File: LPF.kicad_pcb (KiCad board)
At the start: 4 copper layers, 100 x 100 mm, 601 parts, among them J1 Conn_02x05_Counter_Clockwise, P1 SMA, P2 SMA, P3 SMA, P4 SMA, P5 SMA, P6 SMA

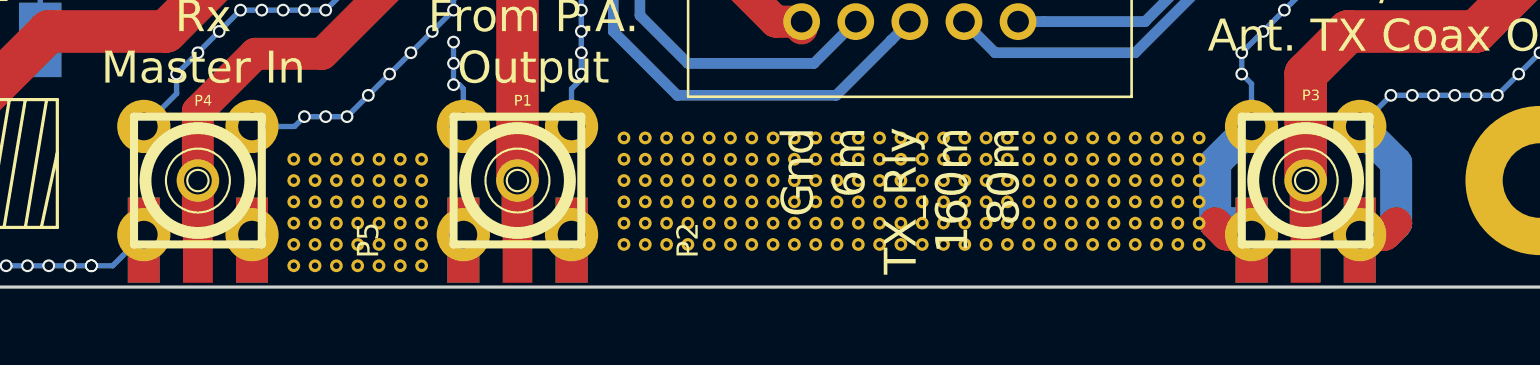
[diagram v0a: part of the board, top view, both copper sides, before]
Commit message: upgrate to Kicad 5.0n, new up to date Gerber
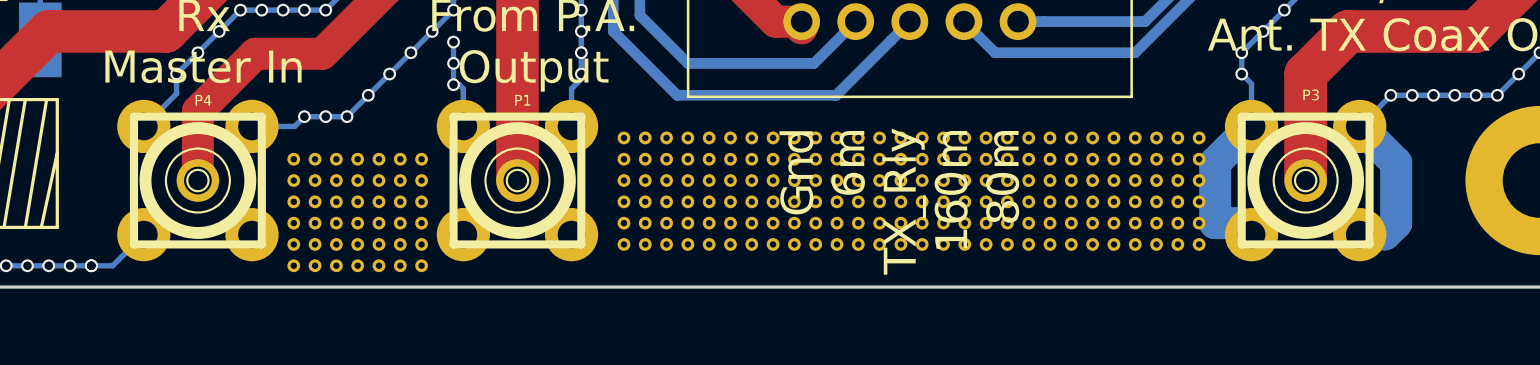
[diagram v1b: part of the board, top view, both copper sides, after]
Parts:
- removed P2, P5, P6: SMA, SMA_PINS:SMA_EDGE_NRW
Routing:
- net GND: track 1547.3 -> 1543.4 mm
- net Net-(P4-Pad1): track 25.8 -> 23.8 mm
- net Net-(P3-Pad1): track 106.4 -> 104.4 mm
- net Net-(P1-Pad1): track 19.9 -> 17.9 mm

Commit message: V 3.0, 54 MHz lpf now online
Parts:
- removed C69: 18p, ATC_B:ATC_500_HandSoldering
- removed REF** (x459): via, via:via
- C11, C27: value C -> 120p
- C16, C18, C29, C41: value C -> 39p
- C17: value 24p -> 4.7p
- C19: value C -> 1000p
- C20, C25: value C -> 470p
- C21: value C -> 330p
- C22, C50, C55: value C -> 82p
- C23, C40: value C -> 68p
- C24: value 31p -> 56p
- C26: value C -> 240p
- C28: value C -> 56p
- C30: value 15p -> 12p
- C31, C35, C36: value C -> 220p
- C32: value C -> 2200p
- C33, C46: value C -> 1100p
- C34: value C -> 680p
- C37, C42: value C -> 180p
- C38: value 68p -> 56p
- C39, C51: value C -> 150p
- C43: value C -> 22p
- C44: value C -> 6.8p
- C45: value 4.7 -> 4.7p
- C47: value C -> 560p
- C48: value C -> 390p
- C49: value C -> 100p
- C59: value 24p -> C (nc)
- L1: value L -> 562nH
- L10: value L -> 4.4uH
- L11: value L -> 2.02uH
- L12: value L -> 1.36uH
- L13: value L -> 351nH
- L14, L16, L6, L9: value L -> 311nH
- L15, L2: value L -> 169nH
- L3: value L -> 3.5uH
- L4: value L -> 1,66uH
- L5: value L -> 1.18uH
- L7: value L -> 235nH
- L8: value L -> 196nH
- moved C59 57.6 mm to (126.5, 117.0), turned to 90 degrees
- moved L15 57.0 mm to (123.0, 119.0), turned to 0 degrees
- moved C45 53.8 mm to (117.5, 120.5), turned to 270 degrees
- moved C15 50.1 mm to (75.0, 116.5), turned to 270 degrees
- moved RL8 50.0 mm to (70.0, 119.0)
- moved D9 49.5 mm to (78.0, 119.0)
- moved L30 43.2 mm to (81.0, 120.0)
- moved C38 40.5 mm to (113.0, 116.5), turned to 270 degrees
- moved L8 34.6 mm to (104.5, 120.0), turned to 45 degrees
- moved C30 27.9 mm to (93.0, 116.5), turned to 0 degrees
- moved RL1 25.9 mm to (66.5, 130.5)
- moved L2 25.2 mm to (87.0, 118.0), turned to 0 degrees
- moved D1 24.3 mm to (60.5, 130.0)
- moved C7 23.7 mm to (63.5, 126.5), turned to 90 degrees
- moved L17 23.0 mm to (68.0, 130.0)
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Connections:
- RL1 pad 13: Net-(C17-Pad1) -> Net-(RL1-Pad13)
- RL1 pad 4: Net-(C17-Pad1) -> Net-(RL1-Pad13)
- RL15 pad 13: Net-(C69-Pad1) -> Net-(C45-Pad2)
- RL15 pad 4: Net-(C69-Pad1) -> Net-(C45-Pad2)
- RL2 pad 8: Net-(C45-Pad2) -> Net-(RL1-Pad13)
- RL2 pad 9: Net-(C45-Pad2) -> Net-(RL1-Pad13)
- RL3 pad 8: Net-(C45-Pad2) -> Net-(RL1-Pad13)
- RL3 pad 9: Net-(C45-Pad2) -> Net-(RL1-Pad13)
- RL4 pad 8: Net-(C45-Pad2) -> Net-(RL1-Pad13)
- RL4 pad 9: Net-(C45-Pad2) -> Net-(RL1-Pad13)
- RL5 pad 8: Net-(C45-Pad2) -> Net-(RL1-Pad13)
- RL5 pad 9: Net-(C45-Pad2) -> Net-(RL1-Pad13)
- RL6 pad 8: Net-(C45-Pad2) -> Net-(RL1-Pad13)
- RL6 pad 9: Net-(C45-Pad2) -> Net-(RL1-Pad13)
- RL7 pad 8: Net-(C45-Pad2) -> Net-(RL1-Pad13)
- RL7 pad 9: Net-(C45-Pad2) -> Net-(RL1-Pad13)
- RL8 pad 13: Net-(C69-Pad1) -> Net-(C17-Pad1)
- RL8 pad 4: Net-(C69-Pad1) -> Net-(C17-Pad1)
- RL8 pad 8: Net-(C45-Pad2) -> Net-(RL1-Pad13)
- RL8 pad 9: Net-(C45-Pad2) -> Net-(RL1-Pad13)
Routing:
- net GND: track 1543.4 -> 568.0 mm, vias 769 -> 1045
- net Net-(C45-Pad2): track 137.5 -> 35.5 mm
- net Net-(RL1-Pad13): track 0.00 -> 94.5 mm
- net Net-(C69-Pad1): track 46.1 -> 0.00 mm
- net 6m_Bypass: track 50.6 -> 81.4 mm
- net +12V: track 93.2 -> 69.0 mm
- net Net-(C30-Pad2): track 17.2 -> 41.2 mm
- net Net-(P1-Pad1): track 17.9 -> 38.5 mm
- net TX_RX_RLY: track 44.8 -> 55.7 mm
- net Net-(C17-Pad2): track 20.7 -> 26.8 mm
- net Net-(P4-Pad1): track 23.8 -> 27.0 mm
- net Net-(C17-Pad1): track 33.6 -> 32.2 mm
- net Net-(C15-Pad1): track 7.26 -> 8.21 mm
- net (no net): vias 0 -> 6
- added copper zone on F.Cu, net GND
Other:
- board text added: "Alexiares LPF V3.0"
- board text removed: "Alexiares LPF V2.0"

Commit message: version 3 provisoire
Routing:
- net GND: vias 1045 -> 1084
- net (no net): vias 6 -> 1
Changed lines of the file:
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@@
-(kicad_pcb (version 20171130) (host pcbnew "(5.0.2)-1")
+(kicad_pcb (version 20171130) (host pcbnew "(5.1.2)-2")
   (general
     (thickness 1.6)
     (drawings 26)
-    (tracks 1917)
+    (tracks 1951)
     (zones 0)
     (modules 138)
@@
   )
   (setup
-    (last_trace_width 3)
+    (last_trace_width 0.25)
     (user_trace_width 0.5)
     (user_trace_width 0.7)
@@
     (zone_45_only no)
     (trace_min 0.2)
-    (segment_width 0.2)
-    (edge_width 0.15)
     (via_size 0.6)
     (via_drill 0.4)
@@
     (uvia_min_size 0.2)
     (uvia_min_drill 0.1)
+    (edge_width 0.15)
+    (segment_width 0.2)
     (pcb_text_width 0.3)
     (pcb_text_size 1.5 1.5)
@@
     (visible_elements 7FFFFE49)
     (pcbplotparams
-      (layerselection 0x010f0_80000007)
+      (layerselection 0x010f0_ffffffff)
       (usegerberextensions true)
       (usegerberattributes false)
       (usegerberadvancedattributes false)
       (creategerberjobfile false)
-      (excludeedgelayer true)
+      (excludeedgelayer false)
       (linewidth 0.100000)
       (plotframeref false)
@@
       (drillshape 0)
       (scaleselection 1)
-      (outputdirectory "Gerber_V2/"))
+      (outputdirectory "Gerber_V3/"))
   )
   (net 0 "")
@@
   (gr_line (start 155 45) (end 55 45) (angle 90) (layer Edge.Cuts) (width 0.15))
   (gr_line (start 155 145) (end 155 45) (angle 90) (layer Edge.Cuts) (width 0.15))
+  (via (at 126 69.5) (size 0.6) (drill 0.4) (layers F.Cu B.Cu) (net 0))
   (via (at 98 113.5) (size 0.6) (drill 0.4) (layers F.Cu B.Cu) (net 1))
   (via (at 99 113.5) (size 0.6) (drill 0.4) (layers F.Cu B.Cu) (net 1))
@@
   (via (at 102 113.5) (size 0.6) (drill 0.4) (layers F.Cu B.Cu) (net 1))
   (via (at 103 113.5) (size 0.6) (drill 0.4) (layers F.Cu B.Cu) (net 1))
-  (via (at 124 125) (size 0.6) (drill 0.4) (layers F.Cu B.Cu) (net 0))
-  (via (at 125 125) (size 0.6) (drill 0.4) (layers F.Cu B.Cu) (net 0))
-  (via (at 126 125) (size 0.6) (drill 0.4) (layers F.Cu B.Cu) (net 0))
-  (via (at 127 125) (size 0.6) (drill 0.4) (layers F.Cu B.Cu) (net 0))
-  (via (at 128 125) (size 0.6) (drill 0.4) (layers F.Cu B.Cu) (net 0))
-  (via (at 126 69.5) (size 0.6) (drill 0.4) (layers F.Cu B.Cu) (net 0))
   (via (at 86 102.25) (size 0.6) (drill 0.4) (layers F.Cu B.Cu) (net 1))
   (via (at 128 92.25) (size 0.6) (drill 0.4) (layers F.Cu B.Cu) (net 1))
@@
   (segment (start 63.5 124.23) (end 64.92 122.81) (width 1) (layer B.Cu) (net 1))
   (segment (start 63.5 125.25) (end 63.5 124.23) (width 1) (layer B.Cu) (net 1))
-  (via (at 129 121) (size 0.6) (drill 0.4) (layers F.Cu B.Cu) (net 1))
   (via (at 129 122) (size 0.6) (drill 0.4) (layers F.Cu B.Cu) (net 1))
   (via (at 129 123) (size 0.6) (drill 0.4) (layers F.Cu B.Cu) (net 1))
   (via (at 129 124) (size 0.6) (drill 0.4) (layers F.Cu B.Cu) (net 1))
-  (via (at 130 125) (size 0.6) (drill 0.4) (layers F.Cu B.Cu) (net 1))
-  (via (at 131 125) (size 0.6) (drill 0.4) (layers F.Cu B.Cu) (net 1))
-  (via (at 132 125) (size 0.6) (drill 0.4) (layers F.Cu B.Cu) (net 1))
-  (via (at 129 125) (size 0.6) (drill 0.4) (layers F.Cu B.Cu) (net 1))
+  (via (at 130 124.75) (size 0.6) (drill 0.4) (layers F.Cu B.Cu) (net 1))
+  (via (at 131 124.75) (size 0.6) (drill 0.4) (layers F.Cu B.Cu) (net 1))
+  (via (at 132 124.75) (size 0.6) (drill 0.4) (layers F.Cu B.Cu) (net 1))
   (via (at 80 125) (size 0.6) (drill 0.4) (layers F.Cu B.Cu) (net 1))
   (via (at 80 126) (size 0.6) (drill 0.4) (layers F.Cu B.Cu) (net 1))
@@
   (via (at 120 126) (size 0.6) (drill 0.4) (layers F.Cu B.Cu) (net 1))
   (via (at 121 126) (size 0.6) (drill 0.4) (layers F.Cu B.Cu) (net 1))
-  (via (at 122 125) (size 0.6) (drill 0.4) (layers F.Cu B.Cu) (net 1))
-  (via (at 123 125) (size 0.6) (drill 0.4) (layers F.Cu B.Cu) (net 1))
+  (via (at 122 125.5) (size 0.6) (drill 0.4) (layers F.Cu B.Cu) (net 1))
+  (via (at 123.25 124.75) (size 0.6) (drill 0.4) (layers F.Cu B.Cu) (net 1))
   (via (at 78.75 124.75) (size 0.6) (drill 0.4) (layers F.Cu B.Cu) (net 1))
   (via (at 77.5 124.75) (size 0.6) (drill 0.4) (layers F.Cu B.Cu) (net 1))
@@
   (via (at 127 112.5) (size 0.6) (drill 0.4) (layers F.Cu B.Cu) (net 1))
   (via (at 129 112) (size 0.6) (drill 0.4) (layers F.Cu B.Cu) (net 1))
+  (via (at 91 104.25) (size 0.6) (drill 0.4) (layers F.Cu B.Cu) (net 1))
+  (via (at 80 104.75) (size 0.6) (drill 0.4) (layers F.Cu B.Cu) (net 1))
+  (via (at 81 104.75) (size 0.6) (drill 0.4) (layers F.Cu B.Cu) (net 1))
+  (via (at 82 104.75) (size 0.6) (drill 0.4) (layers F.Cu B.Cu) (net 1))
+  (via (at 83 104.75) (size 0.6) (drill 0.4) (layers F.Cu B.Cu) (net 1))
+  (via (at 84 104.75) (size 0.6) (drill 0.4) (layers F.Cu B.Cu) (net 1))
+  (via (at 85 104.75) (size 0.6) (drill 0.4) (layers F.Cu B.Cu) (net 1))
+  (via (at 92 104.25) (size 0.6) (drill 0.4) (layers F.Cu B.Cu) (net 1))
+  (via (at 93 104.25) (size 0.6) (drill 0.4) (layers F.Cu B.Cu) (net 1))
+  (via (at 94 104.25) (size 0.6) (drill 0.4) (layers F.Cu B.Cu) (net 1))
+  (via (at 95 104.25) (size 0.6) (drill 0.4) (layers F.Cu B.Cu) (net 1))
+  (via (at 96 104.25) (size 0.6) (drill 0.4) (layers F.Cu B.Cu) (net 1))
+  (via (at 97 104.25) (size 0.6) (drill 0.4) (layers F.Cu B.Cu) (net 1))
+  (via (at 98 104.25) (size 0.6) (drill 0.4) (layers F.Cu B.Cu) (net 1))
+  (via (at 99 104.25) (size 0.6) (drill 0.4) (layers F.Cu B.Cu) (net 1))
+  (via (at 100 104.25) (size 0.6) (drill 0.4) (layers F.Cu B.Cu) (net 1))
+  (via (at 101 104.25) (size 0.6) (drill 0.4) (layers F.Cu B.Cu) (net 1))
+  (via (at 102 104.25) (size 0.6) (drill 0.4) (layers F.Cu B.Cu) (net 1))
+  (via (at 103 104.25) (size 0.6) (drill 0.4) (layers F.Cu B.Cu) (net 1))
+  (via (at 104 104.25) (size 0.6) (drill 0.4) (layers F.Cu B.Cu) (net 1))
+  (via (at 105 104.25) (size 0.6) (drill 0.4) (layers F.Cu B.Cu) (net 1))
+  (via (at 106 104.25) (size 0.6) (drill 0.4) (layers F.Cu B.Cu) (net 1))
+  (via (at 107 104.25) (size 0.6) (drill 0.4) (layers F.Cu B.Cu) (net 1))
+  (via (at 108 104.25) (size 0.6) (drill 0.4) (layers F.Cu B.Cu) (net 1))
+  (via (at 109 104.25) (size 0.6) (drill 0.4) (layers F.Cu B.Cu) (net 1))
+  (via (at 110 104.25) (size 0.6) (drill 0.4) (layers F.Cu B.Cu) (net 1))
+  (via (at 111 104.25) (size 0.6) (drill 0.4) (layers F.Cu B.Cu) (net 1))
+  (via (at 112 104.25) (size 0.6) (drill 0.4) (layers F.Cu B.Cu) (net 1))
+  (via (at 113 104.25) (size 0.6) (drill 0.4) (layers F.Cu B.Cu) (net 1))
+  (via (at 114 104.25) (size 0.6) (drill 0.4) (layers F.Cu B.Cu) (net 1))
+  (via (at 119 104.25) (size 0.6) (drill 0.4) (layers F.Cu B.Cu) (net 1))
+  (via (at 120 104.25) (size 0.6) (drill 0.4) (layers F.Cu B.Cu) (net 1))
+  (via (at 121 104.25) (size 0.6) (drill 0.4) (layers F.Cu B.Cu) (net 1))
+  (via (at 122 104.25) (size 0.6) (drill 0.4) (layers F.Cu B.Cu) (net 1))
+  (via (at 123 104.25) (size 0.6) (drill 0.4) (layers F.Cu B.Cu) (net 1))
+  (via (at 124 104.25) (size 0.6) (drill 0.4) (layers F.Cu B.Cu) (net 1))
+  (via (at 125 104.25) (size 0.6) (drill 0.4) (layers F.Cu B.Cu) (net 1))
+  (via (at 124.5 124.75) (size 0.6) (drill 0.4) (layers F.Cu B.Cu) (net 1))
+  (via (at 125.75 124.75) (size 0.6) (drill 0.4) (layers F.Cu B.Cu) (net 1))
+  (via (at 127 124.75) (size 0.6) (drill 0.4) (layers F.Cu B.Cu) (net 1))
+  (via (at 128 124) (size 0.6) (drill 0.4) (layers F.Cu B.Cu) (net 1))
   (segment (start 85.6 59) (end 125.6 59) (width 0.5) (layer B.Cu) (net 2) (status 10))
   (segment (start 131.95 57.2) (end 136.75 62) (width 0.5) (layer B.Cu) (net 2) (status 20))

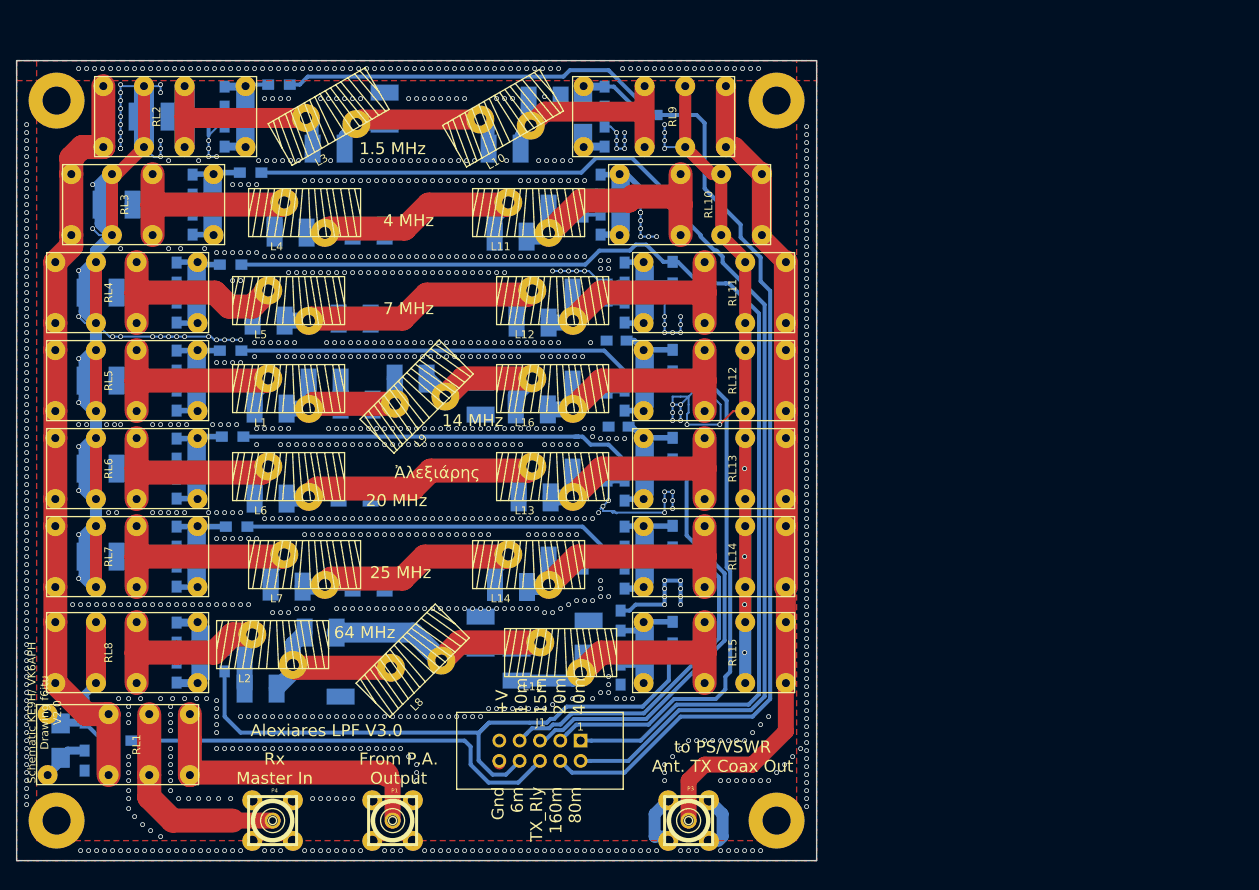
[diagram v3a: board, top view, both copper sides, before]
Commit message: version 4 en dimension 10x15
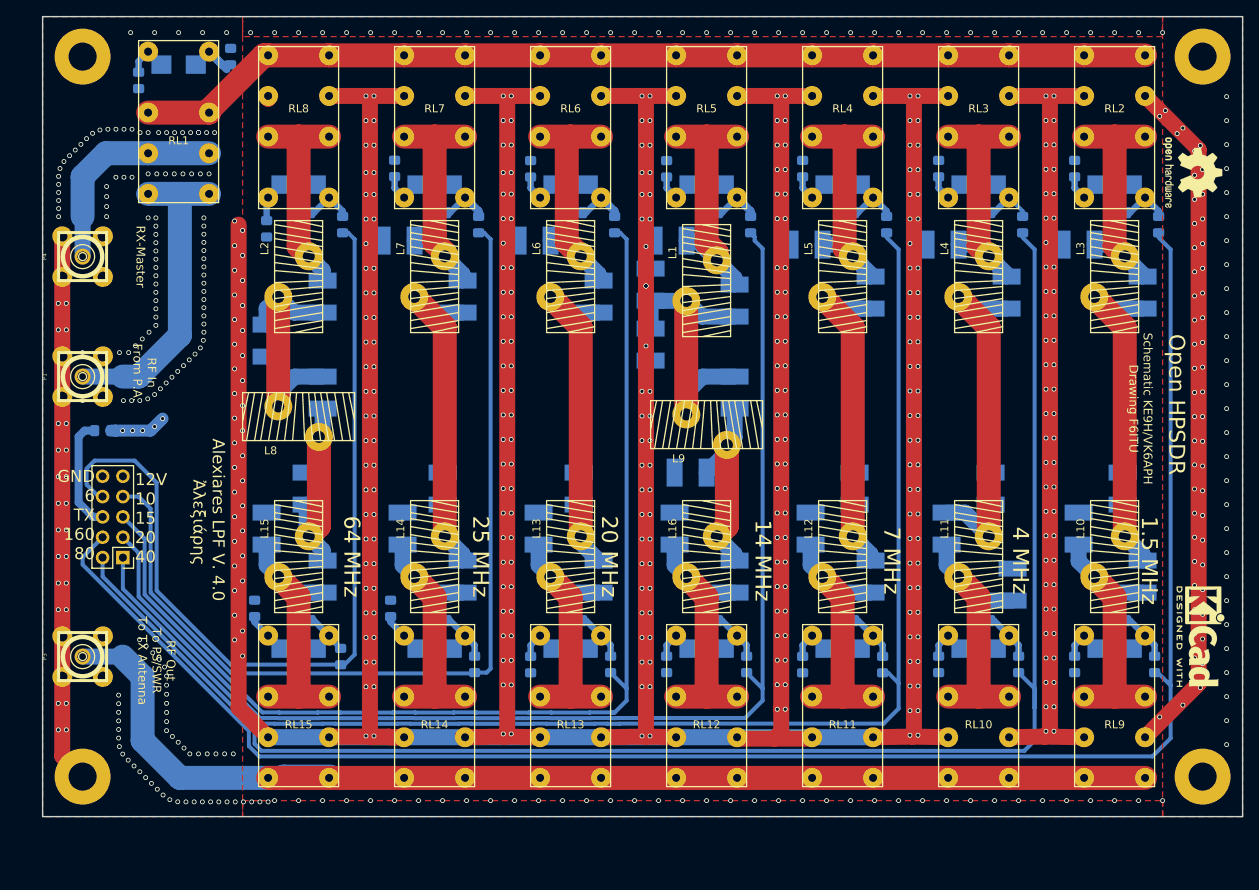
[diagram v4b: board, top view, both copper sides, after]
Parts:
- added REF**: KiCad-Logo2_5mm_SilkScreen, Symbol:KiCad-Logo2_5mm_SilkScreen, F.Cu at (203.0, 117.0)
- added REF**: OSHW-Logo2_9.8x8mm_SilkScreen, Symbol:OSHW-Logo2_9.8x8mm_SilkScreen, F.Cu at (202.0, 59.0)
- C1, C10, C12, C13, C14, C15, C2, C3, C4, C5, C52, C53, C54, C56, C57, C58, C6, C60, C61, C62, C63, C64, C65, C66, C67, C68, C7, C70, C8, C9: footprint Capacitors_SMD:C_0805_HandSoldering -> Capacitor_SMD:C_0805_2012Metric_Pad1.15x1.40mm_HandSolder
- D1, D10, D11, D12, D13, D14, D15, D2, D3, D4, D5, D6, D7, D8, D9: footprint Diodes_SMD:D_SMB -> Diode_SMD:D_SMB
- J1: value Conn_02x05_Counter_Clockwise -> (none); footprint Connectors:IDC_Header_Straight_10pins -> Connector_PinHeader_2.54mm:PinHeader_2x05_P2.54mm_Vertical
- L17, L24, L25, L26, L27, L28, L29, L30, L31, L32, L33, L34, L35, L36, L37: footprint Inductors_SMD:L_0805_HandSoldering -> Inductor_SMD:L_0805_2012Metric_Pad1.15x1.40mm_HandSolder
- TP1, TP2, TP3, TP4: footprint Mounting_Holes:MountingHole_3.5mm_Pad -> MountingHole:MountingHole_3.5mm_Pad
- moved TP3 143.4 mm to (203.2, 134.5), turned to 270 degrees
- moved C61 123.2 mm to (187.2, 120.5), turned to 270 degrees
- moved TP4 121.1 mm to (63.2, 134.5), turned to 270 degrees
- moved C19 116.9 mm to (187.8, 68.0)
- moved RL2 116.3 mm to (192.2, 54.5), turned to 180 degrees
- moved C1 112.7 mm to (192.7, 64.0), turned to 180 degrees
- moved L24 111.3 mm to (197.8, 65.5), turned to 270 degrees
- moved TP2 109.3 mm to (203.2, 44.5), turned to 270 degrees
- moved D3 109.0 mm to (192.2, 60.5), turned to 0 degrees
- moved C8 106.3 mm to (187.2, 58.5)
- moved C32 103.8 mm to (193.2, 98.5)
- moved RL3 103.6 mm to (175.2, 54.5), turned to 180 degrees
- moved C20 103.4 mm to (170.8, 68.0)
- moved C25 103.3 mm to (195.8, 74.0), turned to 270 degrees
- moved L3 100.3 mm to (192.2, 72.0), turned to 270 degrees
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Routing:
- net +12V: track 69.0 -> 475.6 mm
- net GND: track 568.0 -> 894.9 mm, vias 1084 -> 667
- net Net-(C7-Pad1): track 9.22 -> 72.4 mm, vias 0 -> 5
- net 160m: track 161.4 -> 218.9 mm
- net 80m: track 147.8 -> 198.9 mm
- net Net-(P3-Pad1): track 104.4 -> 151.7 mm
- net TX_RX_RLY: track 55.7 -> 14.3 mm
- net Net-(RL1-Pad13): track 94.5 -> 127.8 mm
- net 30/20m: track 124.2 -> 155.4 mm
- net 17/15m: track 110.1 -> 140.2 mm
- net 6m_Bypass: track 81.4 -> 111.3 mm
- net 40m: track 141.6 -> 171.4 mm
- net Net-(C25-Pad2): track 27.0 -> 46.2 mm
- net Net-(C30-Pad2): track 41.2 -> 24.5 mm
- net 12/10m: track 100.5 -> 117.0 mm
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- removed copper zone on In2.Cu, net +12V
- removed copper zone on In1.Cu, net GND
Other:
- board size 100 x 100 mm -> 150 x 100 mm
- board text added: "1.5 MHz 4 MHz 7 MHz 14 MHz"
- board text added: "12V 10 15 20 40"
- board text added: "20 MHz 25 MHz 64 MHz"
- board text added: "Alexiares LPF V. 4.0 Ἀλεξιάρης"
- board text added: "GND 6 TX 160 80"
- board text added: "Open HPSDR"
- board text added: "RF In From P.A."
- board text added: "RF Out To PS/SWR To TX Antenna"
- board text added: "RX-Master"
- board text added: "Schematic KE9H/VK6APH Drawing F6ITU"
- board text removed: "+V 10m 15m 20m 40m"
- board text removed: "1.5 MHz"
- board text removed: "12 Vcc 10m 15m 20m 40m"
- board text removed: "14 MHz"
- board text removed: "20 MHz"
- board text removed: "25 MHz"
- board text removed: "4 MHz"
- board text removed: "64 MHz"
- board text removed: "7 MHz"
- board text removed: "Alexiares LPF"
- board text removed: "Alexiares LPF V3.0"
- board text removed: "From P.A. Output"
- board text removed: "Gnd 6m TX_Rly 160m 80m"
- board text removed: "Gnd 6m-BP TX_Rly 160m 80m"
- board text removed: "RX MASTER_IN"
- board text removed: "Rx Master In"
- board text removed: "Schematic KE9H/ VK6APH Drawing f6itu V2.0"
- board text removed: "to PS/VSWR Ant. TX Coax Out"
- board text removed: "Ἀλεξιάρης"

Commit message: new routing enhancing eddy currents
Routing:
- net GND: track 894.9 -> 885.4 mm, vias 667 -> 665
- net 12/10m: track 117.0 -> 120.4 mm, vias 0 -> 2
- net 160m: track 218.9 -> 221.6 mm, vias 0 -> 3
- net 80m: track 198.9 -> 196.3 mm, vias 0 -> 2
- net 17/15m: track 140.2 -> 140.6 mm, vias 0 -> 2
- net 6m_Bypass: track 111.3 -> 111.5 mm, vias 0 -> 2
- net 40m: track 171.4 -> 171.6 mm, vias 0 -> 2
- net 30/20m: vias 0 -> 2
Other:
- net class Default removed
